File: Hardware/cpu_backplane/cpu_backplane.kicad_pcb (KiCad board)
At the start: 2 copper layers, 149.9 x 99.9 mm, 86 parts, among them J1 USB_B_Micro, J2 Conn_02x02_Odd_Even, J3 Conn_01x06, J4 Conn_01x14, SW1 SW_SPST, U1 74AC161, U2 MAX811SEUS-T, U3 MAX811SEUS-T, U4 PAL24, U5 GAL16V8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

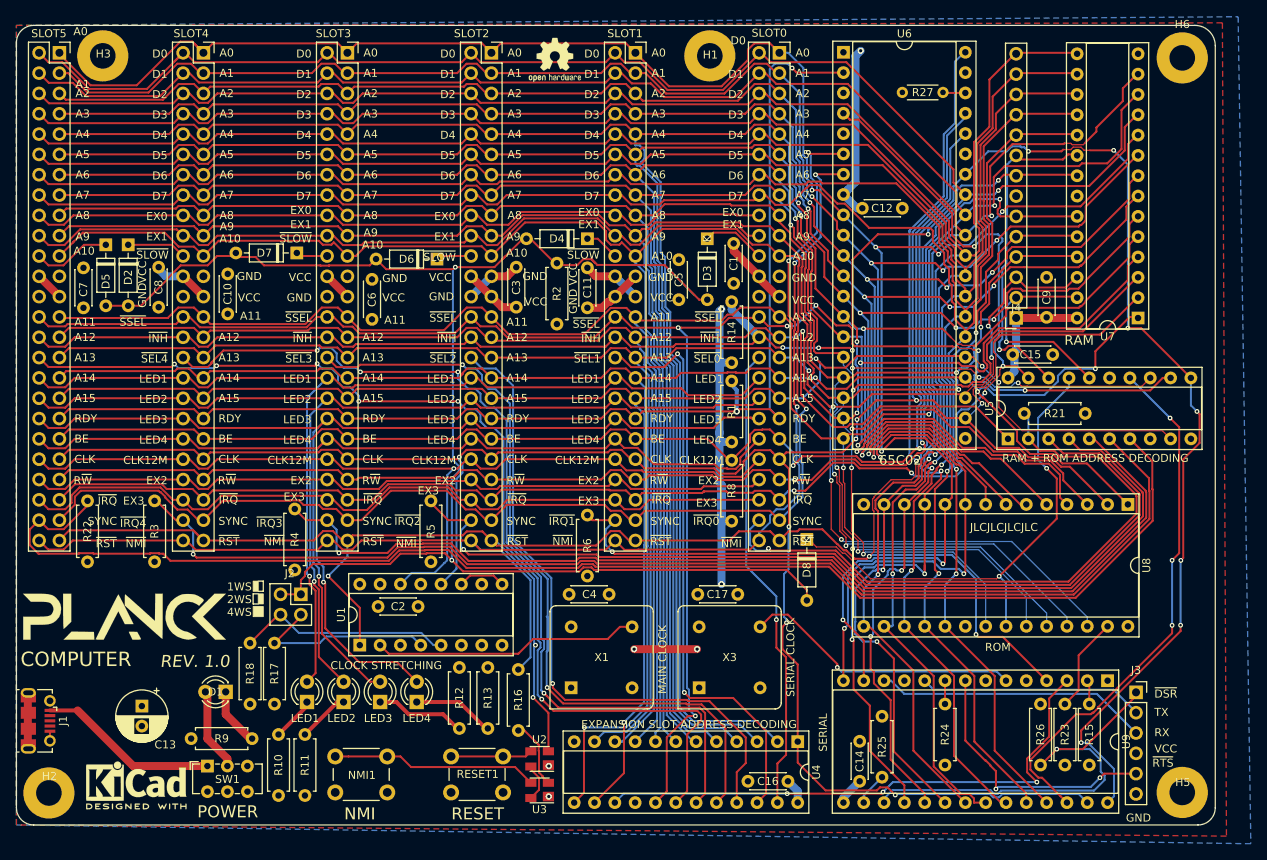
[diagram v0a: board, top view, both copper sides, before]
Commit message: cosmetic fixes to backplane
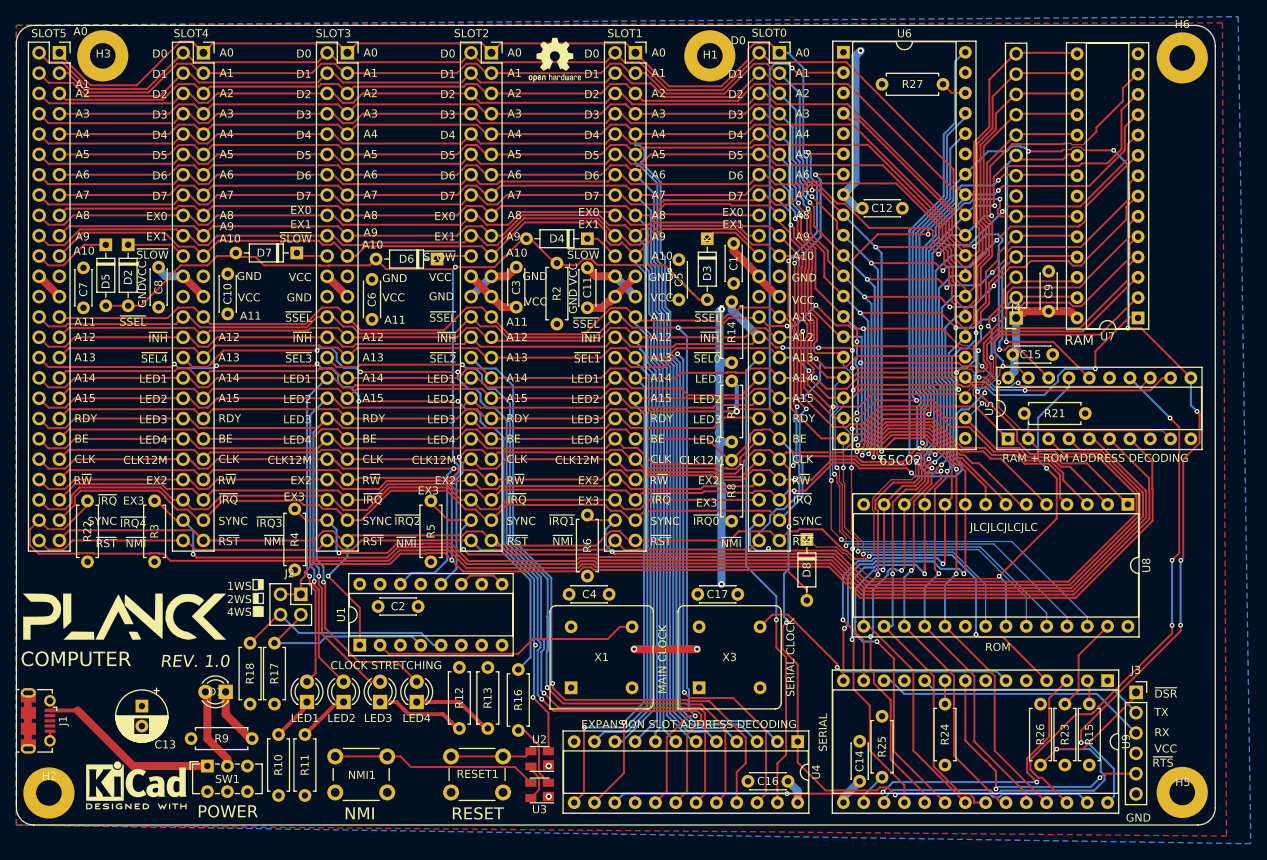
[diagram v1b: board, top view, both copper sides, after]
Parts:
- R27: footprint Resistor_THT:R_Axial_DIN0204_L3.6mm_D1.6mm_P5.08mm_Horizontal -> Resistor_THT:R_Axial_DIN0207_L6.3mm_D2.5mm_P7.62mm_Horizontal
- moved R27 2.74 mm to (108.2, 7.37)
- moved C9 0.80 mm to (129.0, 30.7)
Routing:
- net RDY: track 152.2 -> 153.1 mm
- net +5V: track 143.4 -> 144.1 mm
- net A13: track 257.2 -> 256.5 mm
